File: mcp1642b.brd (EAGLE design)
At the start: 16 x 35 mm, 6 parts, among them U11 MCP1642B

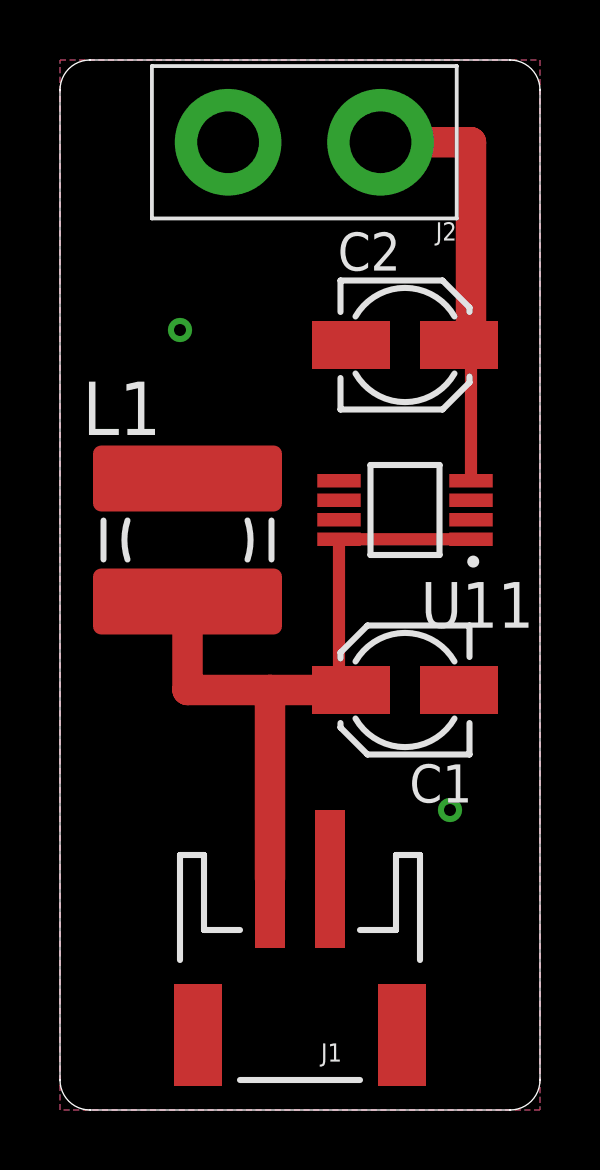
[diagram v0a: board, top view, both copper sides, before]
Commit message: Mon 28 Jan 2019 22:16:21 EST - updated MCP1642 device with planes
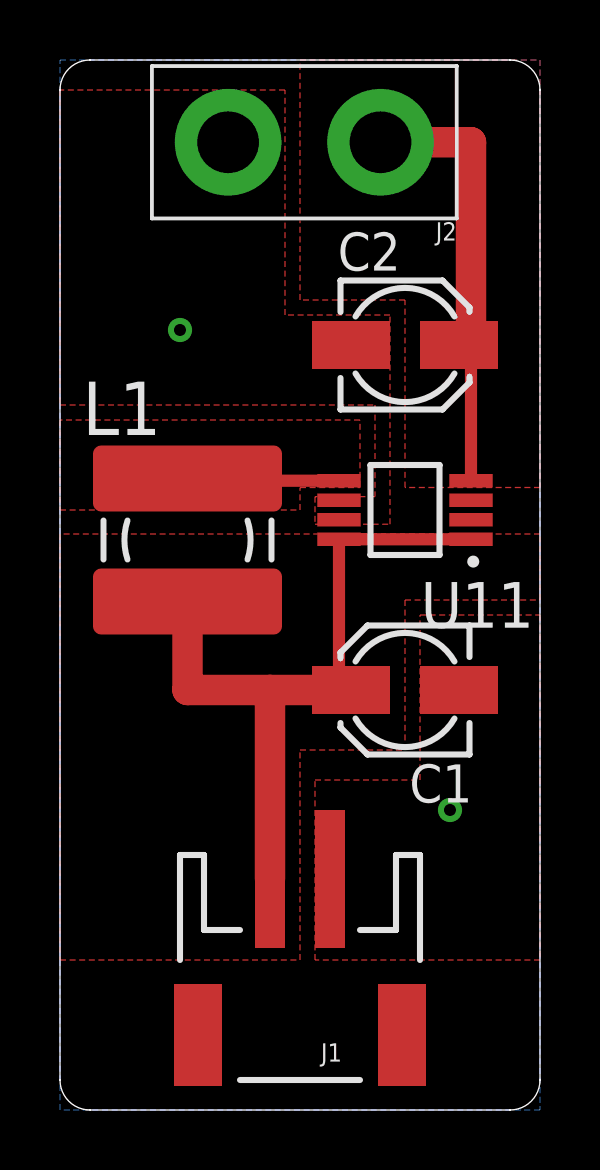
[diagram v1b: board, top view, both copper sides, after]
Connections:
- net N$1 renamed SW
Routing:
- net SW: track 0.00 -> 5.08 mm
- added copper zone on layer 1, net 5V
- added copper zone on layer 1, net SW
- added copper zone on layer 1, net V_BATT
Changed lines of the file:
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@@
 <grid distance="1" unitdist="mm" unit="mm" style="lines" multiple="1" display="yes" altdistance="0.5" altunitdist="mm" altunit="mm"/>
 <layers>
-<layer number="1" name="Top" color="4" fill="1" visible="no" active="yes"/>
+<layer number="1" name="Top" color="4" fill="1" visible="yes" active="yes"/>
 <layer number="2" name="Route2" color="1" fill="3" visible="no" active="no"/>
 <layer number="15" name="Route15" color="4" fill="6" visible="no" active="no"/>
@@
 <layer number="19" name="Unrouted" color="6" fill="1" visible="yes" active="yes"/>
 <layer number="20" name="Dimension" color="24" fill="1" visible="yes" active="yes"/>
-<layer number="21" name="tPlace" color="7" fill="1" visible="no" active="yes"/>
+<layer number="21" name="tPlace" color="7" fill="1" visible="yes" active="yes"/>
 <layer number="22" name="bPlace" color="7" fill="1" visible="yes" active="yes"/>
-<layer number="23" name="tOrigins" color="15" fill="1" visible="no" active="yes"/>
+<layer number="23" name="tOrigins" color="15" fill="1" visible="yes" active="yes"/>
 <layer number="24" name="bOrigins" color="15" fill="1" visible="yes" active="yes"/>
-<layer number="25" name="tNames" color="7" fill="1" visible="no" active="yes"/>
+<layer number="25" name="tNames" color="7" fill="1" visible="yes" active="yes"/>
 <layer number="26" name="bNames" color="7" fill="1" visible="yes" active="yes"/>
 <layer number="27" name="tValues" color="7" fill="1" visible="no" active="yes"/>
@@
 <layer number="37" name="tTest" color="7" fill="1" visible="no" active="yes"/>
 <layer number="38" name="bTest" color="7" fill="1" visible="no" active="yes"/>
-<layer number="39" name="tKeepout" color="4" fill="11" visible="no" active="yes"/>
+<layer number="39" name="tKeepout" color="4" fill="11" visible="yes" active="yes"/>
 <layer number="40" name="bKeepout" color="1" fill="11" visible="yes" active="yes"/>
-<layer number="41" name="tRestrict" color="4" fill="10" visible="no" active="yes"/>
+<layer number="41" name="tRestrict" color="4" fill="10" visible="yes" active="yes"/>
 <layer number="42" name="bRestrict" color="1" fill="10" visible="yes" active="yes"/>
 <layer number="43" name="vRestrict" color="2" fill="10" visible="no" active="yes"/>
@@
 <layer number="49" name="Reference" color="7" fill="1" visible="no" active="yes"/>
 <layer number="50" name="dxf" color="7" fill="1" visible="no" active="no"/>
-<layer number="51" name="tDocu" color="7" fill="1" visible="no" active="yes"/>
+<layer number="51" name="tDocu" color="7" fill="1" visible="yes" active="yes"/>
 <layer number="52" name="bDocu" color="7" fill="1" visible="yes" active="yes"/>
 <layer number="53" name="tGND_GNDA" color="7" fill="9" visible="no" active="no"/>
@@
 <layer number="220" name="220bmp" color="21" fill="1" visible="no" active="no"/>
 <layer number="221" name="221bmp" color="22" fill="1" visible="no" active="no"/>
-<layer number="222" name="222bmp" color="23" fill="1" visible="no" active="no"/>
 <layer number="223" name="223bmp" color="24" fill="1" visible="no" active="no"/>
 <layer number="224" name="224bmp" color="25" fill="1" visible="no" active="no"/>
@@
 <contactref element="C2" pad="-"/>
 <contactref element="J2" pad="2"/>
-<polygon width="0.127" layer="1">
-<vertex x="0" y="35"/>
-<vertex x="16" y="35"/>
-<vertex x="16" y="0"/>
-<vertex x="0" y="0"/>
-</polygon>
 <polygon width="0.127" layer="16">
 <vertex x="0" y="35"/>
@@
 <via x="4" y="26" extent="1-16" drill="0.4"/>
 <via x="13" y="10" extent="1-16" drill="0.4"/>
+<polygon width="0.1524" layer="1" thermals="no">
+<vertex x="8.5" y="20.445"/>
+<vertex x="8.5" y="19.525"/>
+<vertex x="11" y="19.525"/>
+<vertex x="11" y="26.5"/>
+<vertex x="7.5" y="26.5"/>
+<vertex x="7.5" y="34"/>
+<vertex x="0" y="34"/>
+<vertex x="0" y="23.5"/>
+<vertex x="10.5" y="23.5"/>
+<vertex x="10.5" y="20.445"/>
+</polygon>
+<polygon width="0.1524" layer="1" thermals="no">
+<vertex x="16" y="5"/>
+<vertex x="8.5" y="5"/>
+<vertex x="8.5" y="11"/>
+<vertex x="12" y="11"/>
+<vertex x="12" y="16.5"/>
+<vertex x="16" y="16.5"/>
+</polygon>
 </signal>
-<signal name="N$1">
+<signal name="SW">
 <contactref element="U11" pad="SW"/>
 <contactref element="L1" pad="1"/>
-<wire x1="4.25" y1="21.05" x2="9.3" y2="20.975" width="0" layer="19" extent="1-1"/>
+<wire x1="9.3" y1="20.975" x2="4.325" y2="20.975" width="0.4064" layer="1"/>
+<wire x1="4.325" y1="20.975" x2="4.25" y2="21.05" width="0.4064" layer="1"/>
+<polygon width="0.1524" layer="1" thermals="no">
+<vertex x="0" y="20"/>
+<vertex x="8" y="20"/>
+<vertex x="8" y="20.75"/>
+<vertex x="10" y="20.75"/>
+<vertex x="10" y="23"/>
+<vertex x="0" y="23"/>
+</polygon>
 </signal>
 <signal name="V_BATT">
@@
 <wire x1="9.3" y1="19.025" x2="9.3" y2="14" width="0.4064" layer="1"/>
 <wire x1="9.3" y1="14" x2="9.7" y2="14" width="0.4064" layer="1"/>
+<polygon width="0.1524" layer="1" thermals="no">
+<vertex x="0" y="5"/>
+<vertex x="8" y="5"/>
+<vertex x="8" y="12"/>
+<vertex x="11.5" y="12"/>
+<vertex x="11.5" y="17"/>
+<vertex x="16" y="17"/>
+<vertex x="16" y="19.2"/>
+<vertex x="0" y="19.2"/>
+</polygon>
 </signal>
 <signal name="5V">
@@
 <wire x1="10.684" y1="32.258" x2="13.7" y2="32.258" width="1.016" layer="1"/>
 <wire x1="13.7" y1="32.258" x2="13.7" y2="25.5" width="1.016" layer="1"/>
+<polygon width="0.1524" layer="1" thermals="no">
+<vertex x="16" y="20.75"/>
+<vertex x="11.5" y="20.75"/>
+<vertex x="11.5" y="27"/>
+<vertex x="8" y="27"/>
+<vertex x="8" y="35"/>
+<vertex x="16" y="35"/>
+</polygon>
 </signal>
 </signals>
